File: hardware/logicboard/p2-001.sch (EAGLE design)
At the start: 28 parts, among them IC1 5V, IC2 74LS07N, IC3 4066N, K1 G5V1, T1 2SC1815, U1 DS18B20

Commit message: Version 2.0.0 -> 2.0.1
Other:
- note added: "Pineapple II 2.0.1"
- note removed: "Pineapple II 2.0.0"
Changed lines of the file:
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@@
 <sheet>
 <plain>
-<text x="342.9" y="20.32" size="1.778" layer="94">Pineapple II 2.0.0</text>
+<text x="342.9" y="20.32" size="1.778" layer="94">Pineapple II 2.0.1</text>
 </plain>
 <instances>

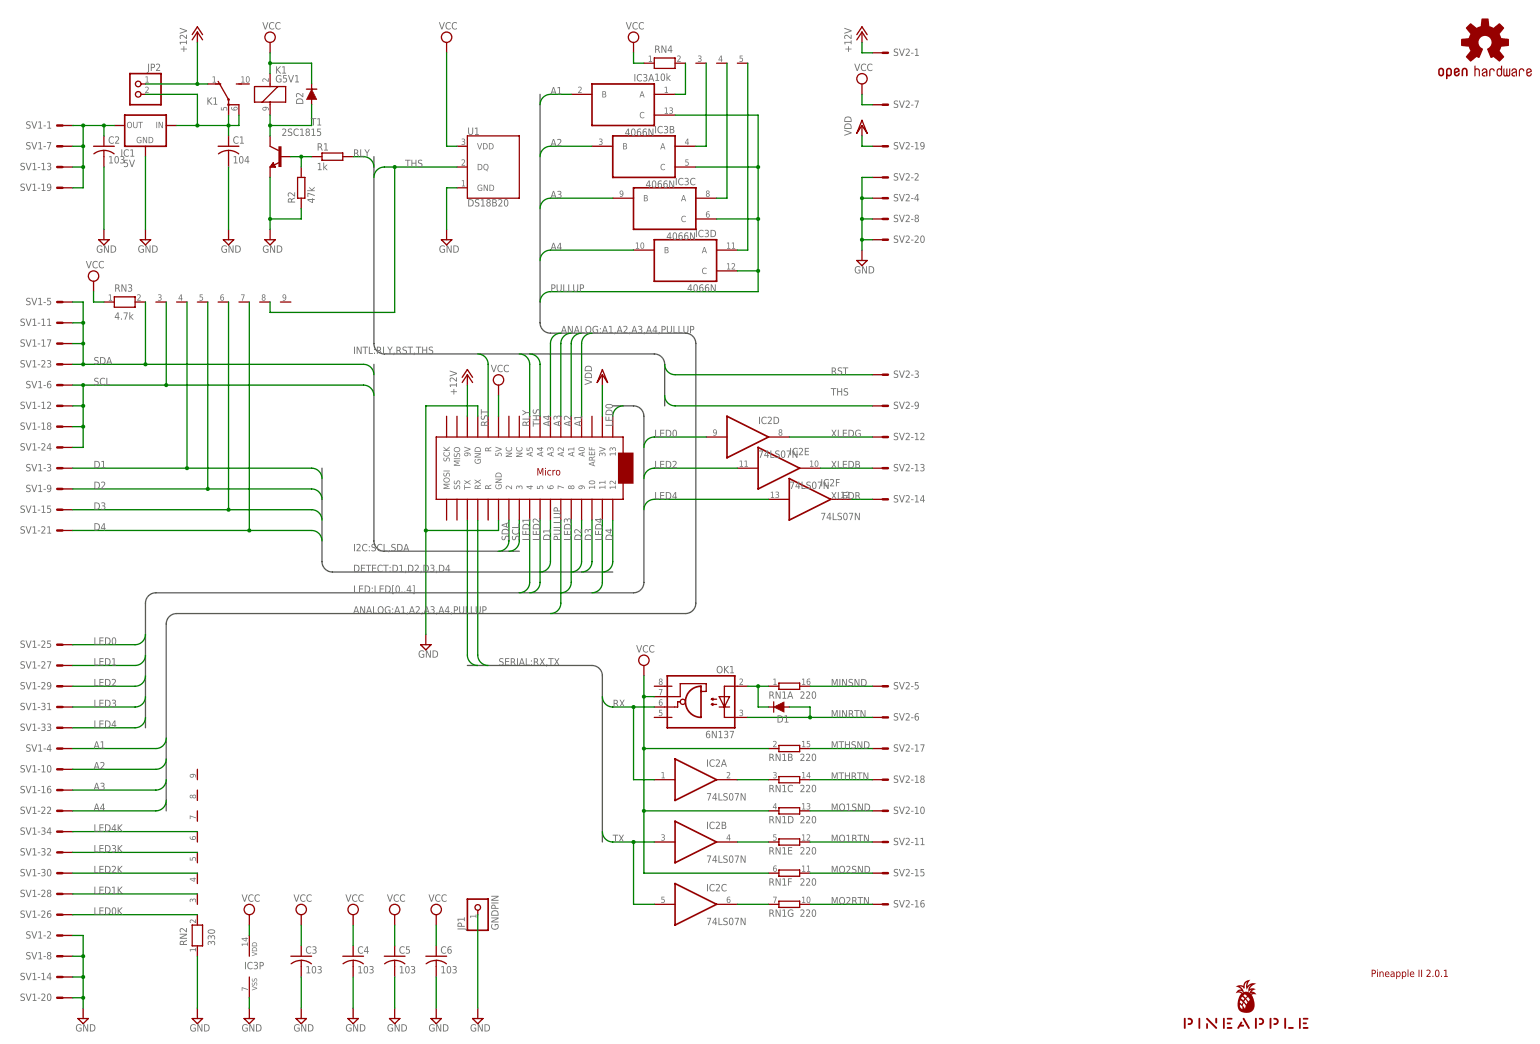
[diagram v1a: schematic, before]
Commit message: Modified schematic and board for the better readability.
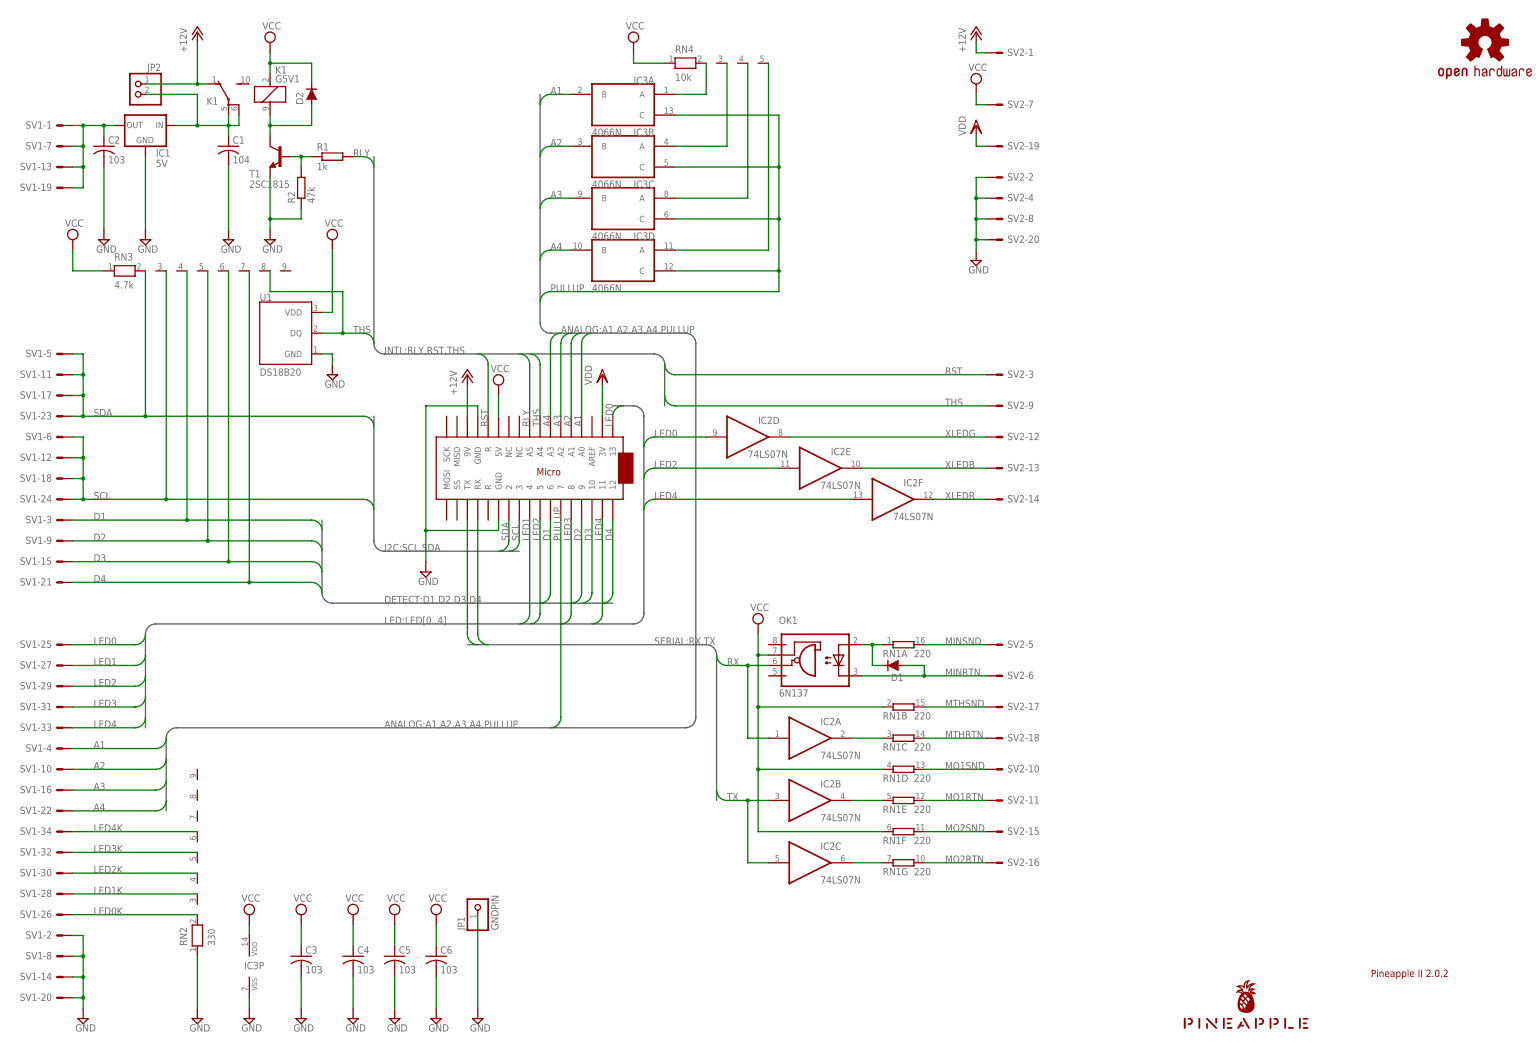
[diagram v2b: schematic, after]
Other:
- note added: "Pineapple II 2.0.2"
- note removed: "Pineapple II 2.0.1"
- moved on the sheet: D1, IC2A, IC2B, IC2C, IC2E, IC2F, IC3B, IC3C, IC3D, OK1, RN1A, RN1B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

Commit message: Real hotfix! Now pull-ups to Analog In are connected to Vout, not Vcc.
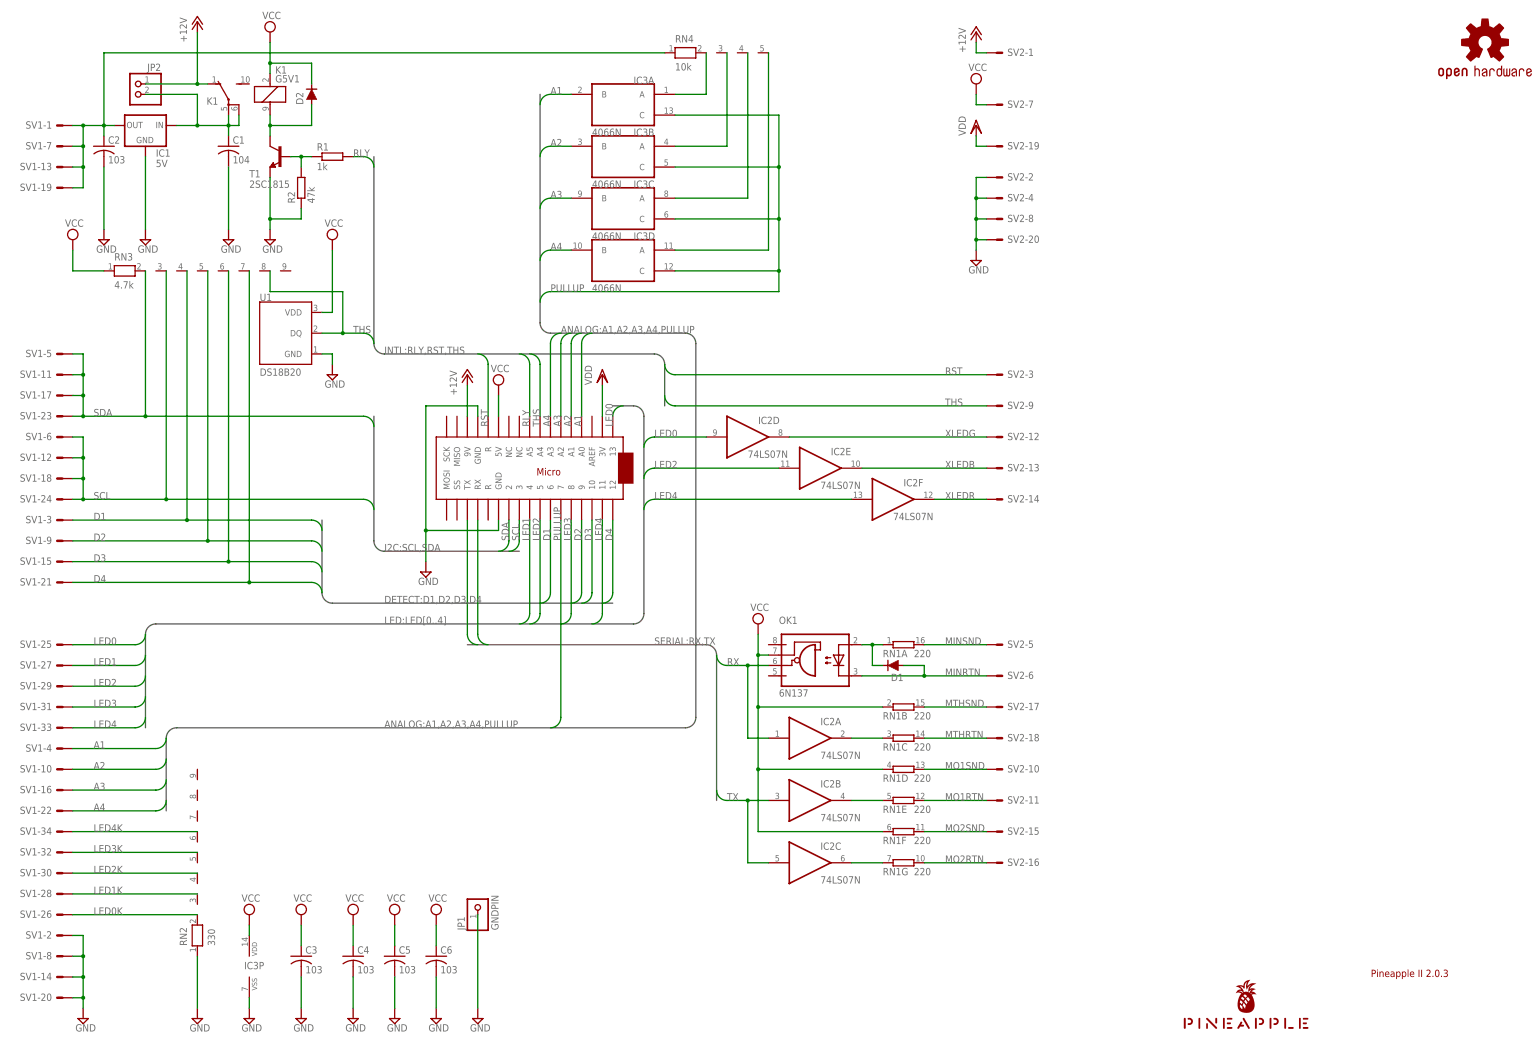
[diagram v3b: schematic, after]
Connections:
- net VCC: no longer RN4.1
- net VOUT: now also RN4.1
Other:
- note added: "Pineapple II 2.0.3"
- note removed: "Pineapple II 2.0.2"
- moved on the sheet: RN4
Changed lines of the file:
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@@
 <setting verticaltext="up"/>
 </settings>
-<grid distance="0.1" unitdist="inch" unit="inch" style="dots" multiple="1" display="yes" altdistance="0.01" altunitdist="inch" altunit="inch"/>
+<grid distance="0.1" unitdist="inch" unit="inch" style="lines" multiple="1" display="no" altdistance="0.01" altunitdist="inch" altunit="inch"/>
 <layers>
 <layer number="1" name="Top" color="4" fill="1" visible="no" active="no"/>
@@
 <part name="JP1" library="pinhead" library_urn="urn:adsk.eagle:library:325" deviceset="PINHD-1X1" device="" package3d_urn="urn:adsk.eagle:package:22485/2" value="GNDPIN"/>
 <part name="SUPPLY23" library="supply2" deviceset="GND" device=""/>
-<part name="SUPPLY24" library="supply2" library_urn="urn:adsk.eagle:library:372" deviceset="VCC" device=""/>
 <part name="RN4" library="resistor-net" library_urn="urn:adsk.eagle:library:343" deviceset="RN04" device="" package3d_urn="urn:adsk.eagle:package:24976/1" value="10k"/>
 <part name="IC3" library="40xx" library_urn="urn:adsk.eagle:library:80" deviceset="4066" device="N" package3d_urn="urn:adsk.eagle:package:16407/2"/>
@@
 <sheet>
 <plain>
-<text x="342.9" y="20.32" size="1.778" layer="94">Pineapple II 2.0.2</text>
+<text x="342.9" y="20.32" size="1.778" layer="94">Pineapple II 2.0.3</text>
 </plain>
 <instances>
@@
 <attribute name="VALUE" x="61.595" y="197.485" size="1.778" layer="96"/>
 </instance>
-<instance part="P+1" gate="1" x="55.88" y="251.46" smashed="yes">
-<attribute name="VALUE" x="53.34" y="246.38" size="1.778" layer="96" rot="R90"/>
+<instance part="P+1" gate="1" x="55.88" y="254" smashed="yes">
+<attribute name="VALUE" x="53.34" y="248.92" size="1.778" layer="96" rot="R90"/>
 </instance>
 <instance part="P+2" gate="1" x="121.92" y="167.64" smashed="yes">
@@
 <attribute name="PART" x="60.96" y="233.68" size="1.778" layer="95" rot="MR0"/>
 </instance>
-<instance part="SUPPLY6" gate="G$1" x="73.66" y="248.92" smashed="yes">
-<attribute name="VALUE" x="71.755" y="252.095" size="1.778" layer="96"/>
+<instance part="SUPPLY6" gate="G$1" x="73.66" y="251.46" smashed="yes">
+<attribute name="VALUE" x="71.755" y="254.635" size="1.778" layer="96"/>
 </instance>
 <instance part="T1" gate="G$1" x="76.2" y="220.98" smashed="yes" rot="MR0">
@@
 <attribute name="VALUE" x="122.555" y="6.985" size="1.778" layer="96"/>
 </instance>
-<instance part="SUPPLY24" gate="G$1" x="162.56" y="248.92" smashed="yes">
-<attribute name="VALUE" x="160.655" y="252.095" size="1.778" layer="96"/>
-</instance>
-<instance part="RN4" gate="1" x="175.26" y="243.84" smashed="yes">
-<attribute name="NAME" x="172.72" y="246.38" size="1.778" layer="95"/>
-<attribute name="VALUE" x="172.72" y="239.522" size="1.778" layer="96"/>
+<instance part="RN4" gate="1" x="175.26" y="246.38" smashed="yes">
+<attribute name="NAME" x="172.72" y="248.92" size="1.778" layer="95"/>
+<attribute name="VALUE" x="172.72" y="242.062" size="1.778" layer="96"/>
 </instance>
 <instance part="IC3" gate="A" x="160.02" y="233.68" smashed="yes" rot="MR0">
@@
 <pinref part="SUPPLY6" gate="G$1" pin="VCC"/>
 <pinref part="K1" gate="1" pin="1"/>
-<wire x1="73.66" y1="246.38" x2="73.66" y2="243.84" width="0.1524" layer="91"/>
+<wire x1="73.66" y1="248.92" x2="73.66" y2="243.84" width="0.1524" layer="91"/>
 <pinref part="D2" gate="G$1" pin="C"/>
 <wire x1="73.66" y1="243.84" x2="73.66" y2="241.3" width="0.1524" layer="91"/>
@@
 <pinref part="RN3" gate="1" pin="1"/>
 <wire x1="33.02" y1="193.04" x2="25.4" y2="193.04" width="0.1524" layer="91"/>
-</segment>
-<segment>
-<pinref part="SUPPLY24" gate="G$1" pin="VCC"/>
-<wire x1="162.56" y1="246.38" x2="162.56" y2="243.84" width="0.1524" layer="91"/>
-<pinref part="RN4" gate="1" pin="1"/>
-<wire x1="162.56" y1="243.84" x2="170.18" y2="243.84" width="0.1524" layer="91"/>
 </segment>
 <segment>
@@
 <pinref part="P+1" gate="1" pin="+12V"/>
 <pinref part="K1" gate="2" pin="O"/>
-<wire x1="55.88" y1="248.92" x2="55.88" y2="238.76" width="0.1524" layer="91"/>
+<wire x1="55.88" y1="251.46" x2="55.88" y2="238.76" width="0.1524" layer="91"/>
 <wire x1="55.88" y1="238.76" x2="58.42" y2="238.76" width="0.1524" layer="91"/>
 <pinref part="JP2" gate="G$1" pin="1"/>
@@
 <wire x1="27.94" y1="213.36" x2="27.94" y2="218.44" width="0.1524" layer="91"/>
 <junction x="27.94" y="218.44"/>
+<pinref part="RN4" gate="1" pin="1"/>
+<wire x1="33.02" y1="246.38" x2="170.18" y2="246.38" width="0.1524" layer="91"/>
+<wire x1="33.02" y1="246.38" x2="33.02" y2="228.6" width="0.1524" layer="91"/>
 </segment>
 </net>
@@
 <segment>
 <pinref part="RN4" gate="1" pin="2"/>
-<wire x1="180.34" y1="243.84" x2="180.34" y2="236.22" width="0.1524" layer="91"/>
+<wire x1="180.34" y1="246.38" x2="180.34" y2="236.22" width="0.1524" layer="91"/>
 <pinref part="IC3" gate="A" pin="A"/>
 <wire x1="180.34" y1="236.22" x2="172.72" y2="236.22" width="0.1524" layer="91"/>
@@
 <segment>
 <pinref part="RN4" gate="1" pin="3"/>
-<wire x1="185.42" y1="243.84" x2="185.42" y2="223.52" width="0.1524" layer="91"/>
+<wire x1="185.42" y1="246.38" x2="185.42" y2="223.52" width="0.1524" layer="91"/>
 <pinref part="IC3" gate="B" pin="A"/>
 <wire x1="185.42" y1="223.52" x2="172.72" y2="223.52" width="0.1524" layer="91"/>
@@
 <pinref part="RN4" gate="1" pin="4"/>
 <pinref part="IC3" gate="C" pin="A"/>
-<wire x1="190.5" y1="243.84" x2="190.5" y2="210.82" width="0.1524" layer="91"/>
+<wire x1="190.5" y1="246.38" x2="190.5" y2="210.82" width="0.1524" layer="91"/>
 <wire x1="190.5" y1="210.82" x2="172.72" y2="210.82" width="0.1524" layer="91"/>
 </segment>
@@
 <pinref part="RN4" gate="1" pin="5"/>
 <pinref part="IC3" gate="D" pin="A"/>
-<wire x1="195.58" y1="243.84" x2="195.58" y2="198.12" width="0.1524" layer="91"/>
+<wire x1="195.58" y1="246.38" x2="195.58" y2="198.12" width="0.1524" layer="91"/>
 <wire x1="195.58" y1="198.12" x2="172.72" y2="198.12" width="0.1524" layer="91"/>
 </segment>

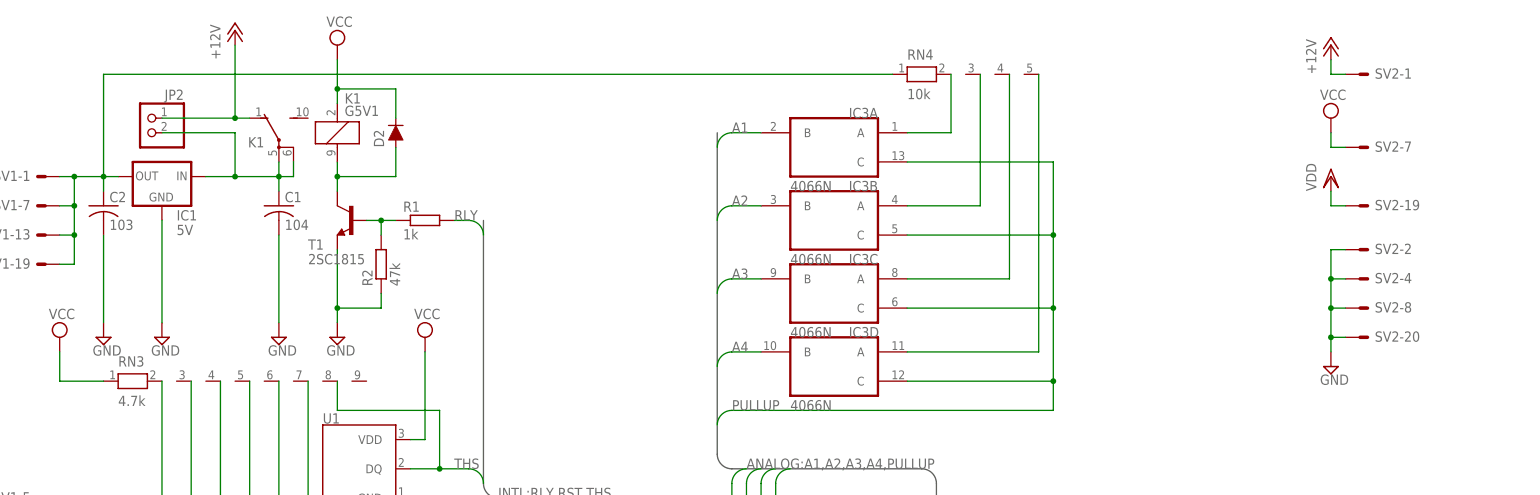
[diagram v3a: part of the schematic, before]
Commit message: Added pull-up selector.
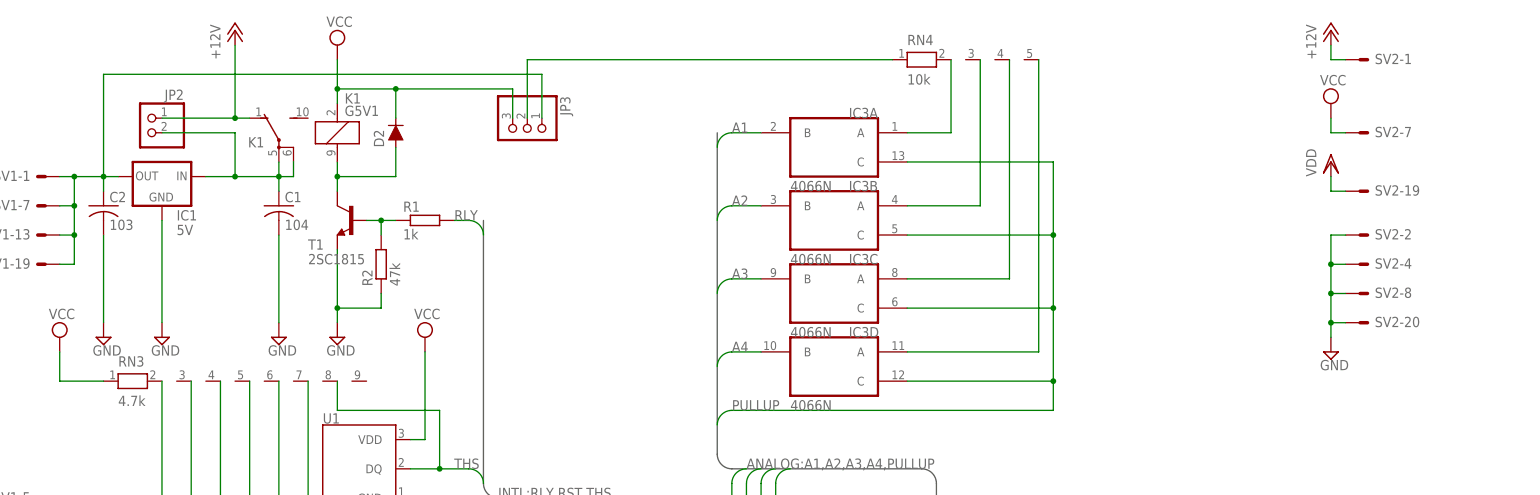
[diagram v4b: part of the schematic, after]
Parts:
- added JP3: (no value), pinhead:PINHD-1X3
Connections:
- net 12VRLY renamed N$1
- new net N$2: JP3.2, RN4.1
- net VCC: now also JP3.3
- net VOUT: now also JP3.1; no longer RN4.1
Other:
- moved on the sheet: RN4, SV2-1, SV2-19, SV2-2, SV2-20, SV2-4, SV2-7, SV2-8
